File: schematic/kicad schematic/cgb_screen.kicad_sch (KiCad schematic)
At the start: 28 parts, among them Q1 2SA1576A, U10 UMZ2N, U4 CGB_REG, U9 HN1L02FU

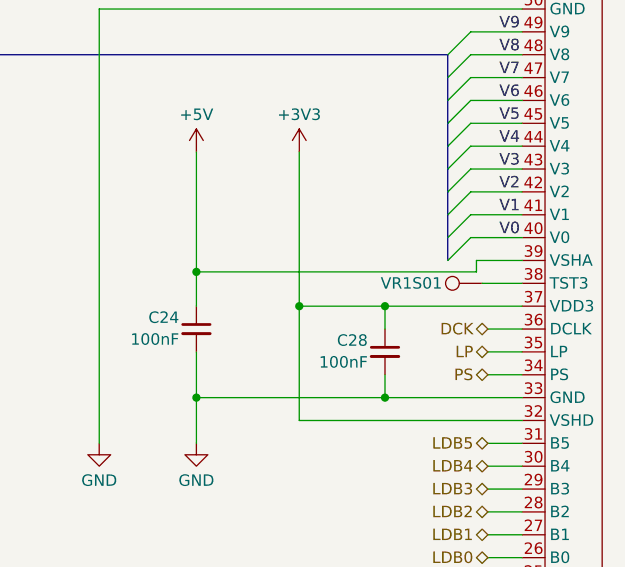
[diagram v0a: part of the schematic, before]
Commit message: fixed schematic, thx giltesa and darren
the ir transistor was labelled wrong
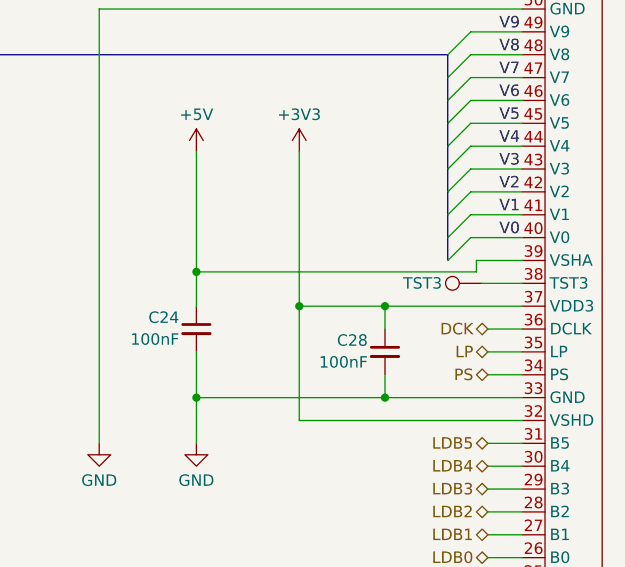
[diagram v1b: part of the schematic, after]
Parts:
- renumbered VR1S01 to TST3
